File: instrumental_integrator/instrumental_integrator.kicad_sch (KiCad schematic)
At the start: 43 parts, among them CN1 282841-2, Q1 2N7002, U1 INA128, U3 LTC2358-16, U4 BAT54_C2926171, U5 BAT54_C2926171, U6 BAT54_C2926171, U7 BAT54_C2926171, U9 TLV2387DR

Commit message: added footprint links and changed instr opamp to ina828
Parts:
- removed RV1: R_Potentiometer, symbol Device:R_Potentiometer
- removed U1: INA128, symbol Amplifier_Instrumentation:INA128
- added LED1: LTST-C170GKT, easyeda2kicad:LED0805-RD_GREEN, symbol easyeda2kicad:LTST-C170GKT
- added LED5: LTST-C170TBKT, easyeda2kicad:LED0805-RD_BLUE, symbol easyeda2kicad:LTST-C170TBKT
- added LED6: LTST-C170KRKT, easyeda2kicad:LED0805-R-RD, symbol easyeda2kicad:LTST-C170KRKT
- added R27, R28: 50, symbol Device:R
- added R29: 300, symbol Device:R
- added U1: INA828IDR, easyeda2kicad:SOIC-8_L4.9-W3.9-P1.27-LS6.0-BL, symbol easyeda2kicad:INA828IDR
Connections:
- net +2V5: now also LED5.2 (A), U1.7 (+VS)
- net +5V: now also LED1.2 (+)
- net -2V5: now also LED6.2 (-), U1.4 (-VS)
- net GND: now also U3.3 (IN5-), R27.2, R28.2, R29.2, U1.5 (REF)
- net IN1: now also U1.2 (-IN)
- net IN2: now also U1.3 (+IN)
- net gain_out: now also U3.4 (IN5+)
- net at C16.1, C17.2: now also U1.6 (OUT)
- new net: LED1.1 (-), R29.1
- new net: LED5.1 (K), R27.1
- new net: LED6.1 (+), R28.1
- new net resistor chain/rg1: U1.1 (RG)
- new net resistor chain/rg2: U1.8 (RG)
- no-connect marks 51 -> 49
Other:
- added sheet resistor chain (resistorchain.kicad_sch)
- moved on the sheet: C16, C17, C2, C3, R13

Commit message: added testpoints adn +- 15V rails and resistor chain asw from previous iteration
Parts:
- added CN2: 282841-2, easyeda2kicad:CONN-TH_2P-P5.08_282841-2, symbol easyeda2kicad:282841-2
- added J1, J3, J4, J5, J6, J7, J8: Conn_01x01_Socket, TestPoint:TestPoint_THTPad_1.0x1.0mm_Drill0.5mm, symbol Connector:Conn_01x01_Socket
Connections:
- net +2V5: no longer C6.1, U3.16 (VCC)
- net +3.3V: now also H2.5
- net +5V: now also C8.2, U3.42 (VDD), U3.43 (VDD)
- net -2V5: no longer C10.1, U3.17 (VEE), U3.45 (VEE)
- net A_out: now also J7.1 (Pin_1)
- net IN1: now also CN2.1
- net IN2: now also CN2.2
- net gain_out: now also J6.1 (Pin_1)
- net intout: now reaches C1.2, Q1.3 (D), R5.2, R9.2, U9.1 (OUT1)
- net intout: now also J8.1 (Pin_1)
- net resistor chain/rg1 renamed rg1
- net rg1: now also J4.1 (Pin_1)
- net resistor chain/rg2 renamed rg2
- net rg2: now also J5.1 (Pin_1)
- new net +15V: C6.1, J1.1 (Pin_1), U3.16 (VCC)
- new net -15V: C10.1, J3.1 (Pin_1), U3.17 (VEE), U3.45 (VEE)
- no-connect marks 49 -> 48
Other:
- sheet power ports: added +15V, -15V; removed none
- note added: "Debug Test Points"
- note added: "Power LEDs"
- moved on the sheet: C8

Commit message: changed adc
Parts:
- removed C6: 0.1u, symbol Device:C
- removed C7, C8: 100n, symbol Device:C
- removed U3: LTC2358-16, Package_QFP:LQFP-48_7x7mm_P0.5mm, symbol Analog_ADC:LTC2358-16
- added C24: C_Polarized_Small_US, symbol Device:C_Polarized_Small_US
- added C25: 10uF, symbol Device:C
- added J9: Conn_Coaxial, symbol Connector:Conn_Coaxial
- added SW2: SW_DPST, symbol Switch:SW_DPST
- added SW4, SW7: SW_MEC_5G, symbol Switch:SW_MEC_5G
- added U10: ADS8681RUM, Package_DFN_QFN:QFN-16-1EP_4x4mm_P0.65mm_EP2.7x2.7mm, symbol Analog_ADC:ADS8681RUM
- C10: value 0.1u -> 10uF
- C11: value 0.1u -> 4.7uF
- C12: value 47u -> 10uF
- C9: value 2.2u -> 1uF
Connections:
- net +3.3V: now also C12.1, U10.14 (DVDD)
- net +5V: now also C25.1, U10.16 (AVDD)
- net -15V: no longer C10.1
- net A_out: now also C24.1, SW2.2, SW7.3 (B), SW7.4 (B), U10.5 (AIN_P); no longer C13.1, R9.1
- net GND: now also C10.1, C11.2, C24.2, C25.2, J9.2 (Ext), U10.1 (AGND), U10.15 (DGND), U10.17 (PAD), U10.3 (REFGND), U10.6 (AIN_GND), U10.7 (~{RST}); no longer C10.2, C11.1
- net GP16: now also J9.1 (In)
- net GP2: now also U10.10 (SCLK)
- net GP3: now also U10.8 (SDI)
- net GP4: now also U10.11 (SDO-0)
- net GP5: now also U10.12 (SDO-1)
- net GP6: now also U10.9 (CONVST/~{CS}); no longer R10.2
- net GP7: now also U10.13 (RVS)
- net GP8: now also R10.2
- net RUN: now also SW4.1 (A), SW4.2 (A); no longer H2.11
- net gain_out: now also SW2.3, SW7.1 (A), SW7.2 (A); no longer R3.1
- net at C9.2: now also C10.2, U10.4 (REFCAP)
- new net: R3.1, SW2.4
- new net: H2.11, SW4.3 (B), SW4.4 (B)
- new net: C11.1, U10.2 (REFIO)
- new net switchin: C13.1, R9.1, SW2.1
- no-connect marks 48 -> 23
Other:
- note added: "Rogowski RP2040 Connection"
- note added: "Violet Bustos Allen Chen"
- note removed: "Rogowski - Pico connection"
- note removed: "Schem by violet bustos"
- moved on the sheet: C1, C13, C14, C15, C16, C17, C2, C3, C4, C5, CN1, CN2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

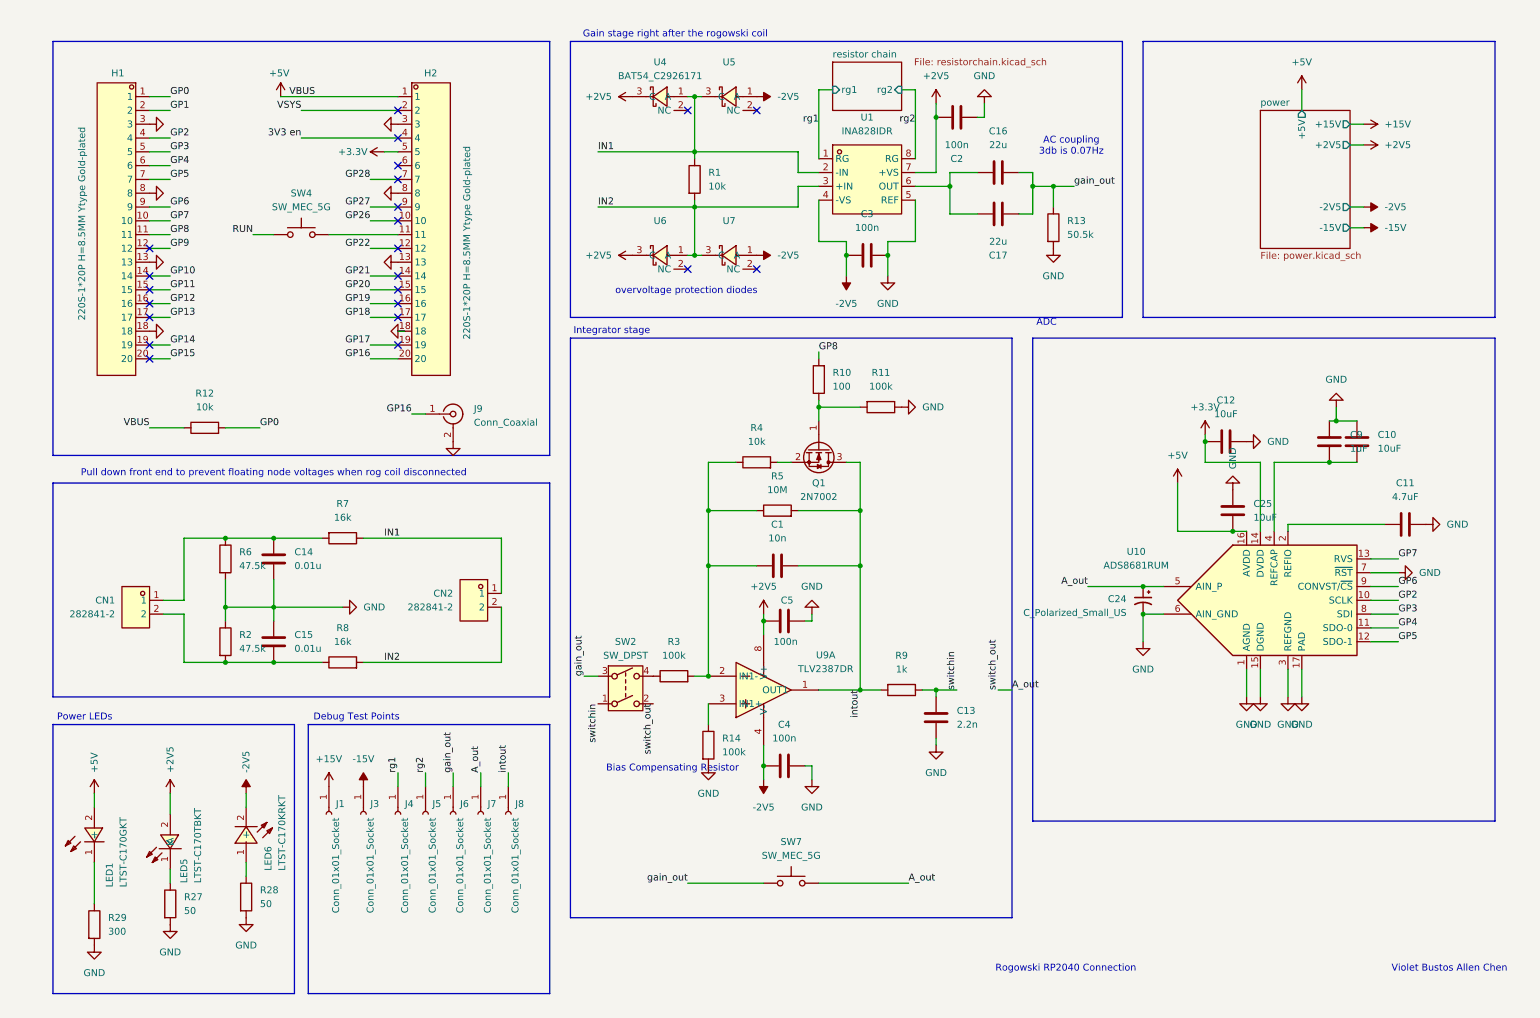
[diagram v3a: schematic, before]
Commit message: switch footprints
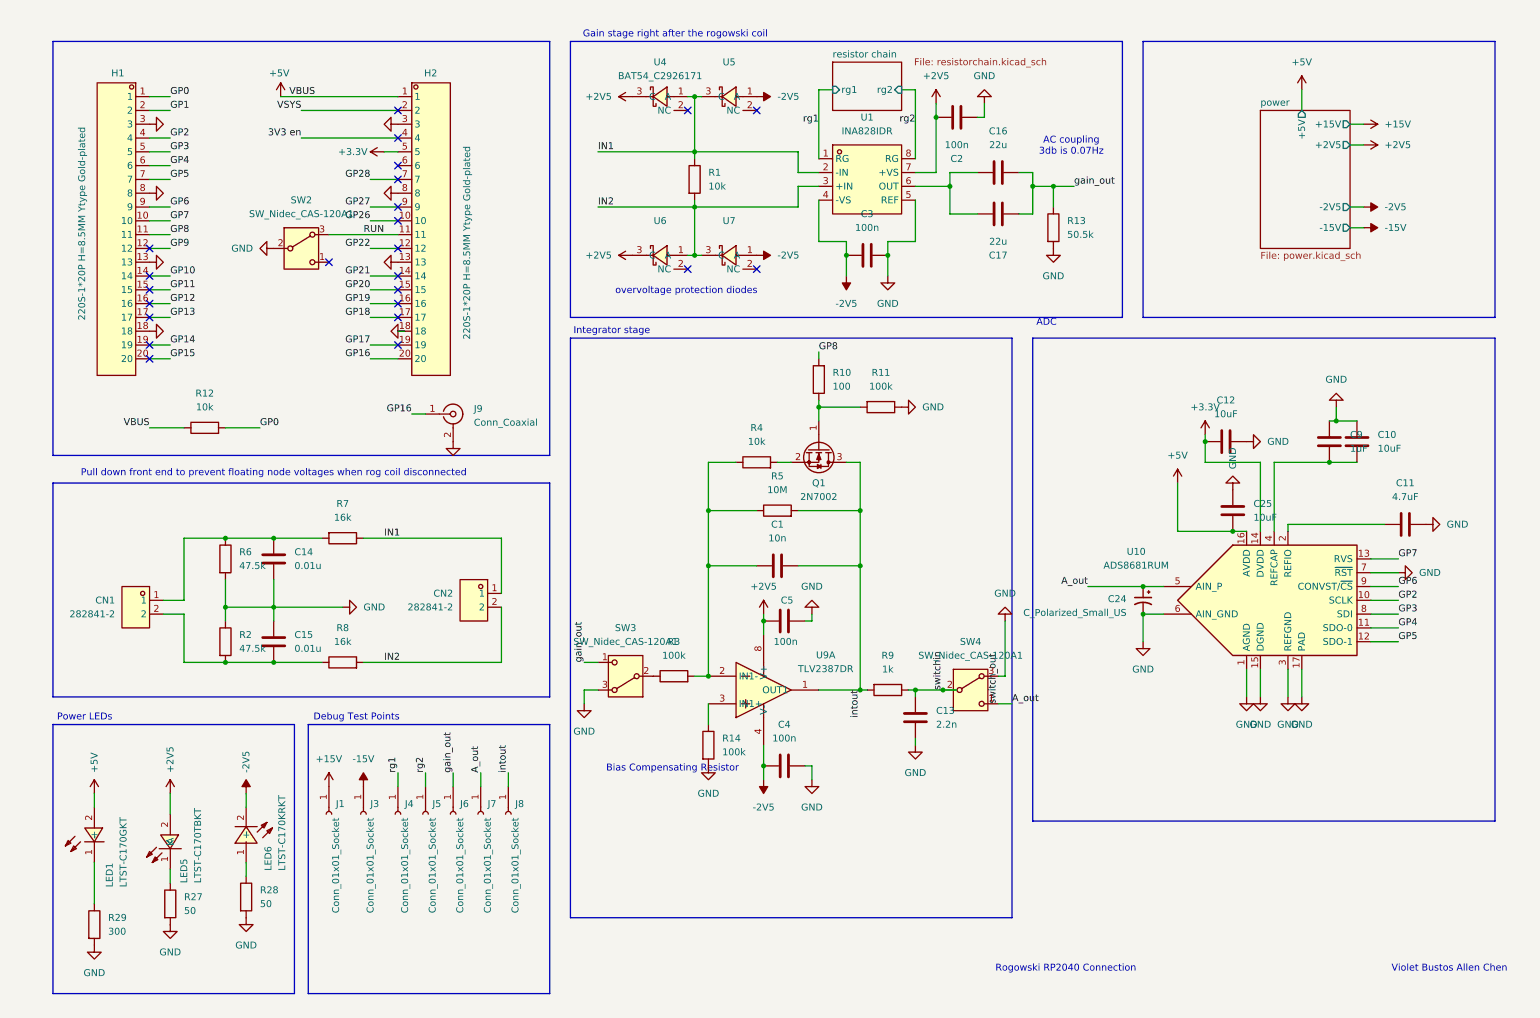
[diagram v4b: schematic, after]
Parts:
- removed SW2: SW_DPST, symbol Switch:SW_DPST
- removed SW4, SW7: SW_MEC_5G, symbol Switch:SW_MEC_5G
- added SW2, SW3, SW4: SW_Nidec_CAS-120A1, Button_Switch_SMD:Nidec_Copal_CAS-120A, symbol Switch:SW_Nidec_CAS-120A1
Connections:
- net A_out: now also SW4.1 (C)
- net GND: now also SW2.2 (B), SW3.3 (A), SW4.3 (A)
- net RUN: now also H2.11, SW2.3 (A)
- net gain_out: now also SW3.1 (C)
- net switchin: now also SW4.2 (B)
- net at R3.1: now also SW3.2 (B)
- no-connect marks 23 -> 24
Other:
- moved on the sheet: C13, R9

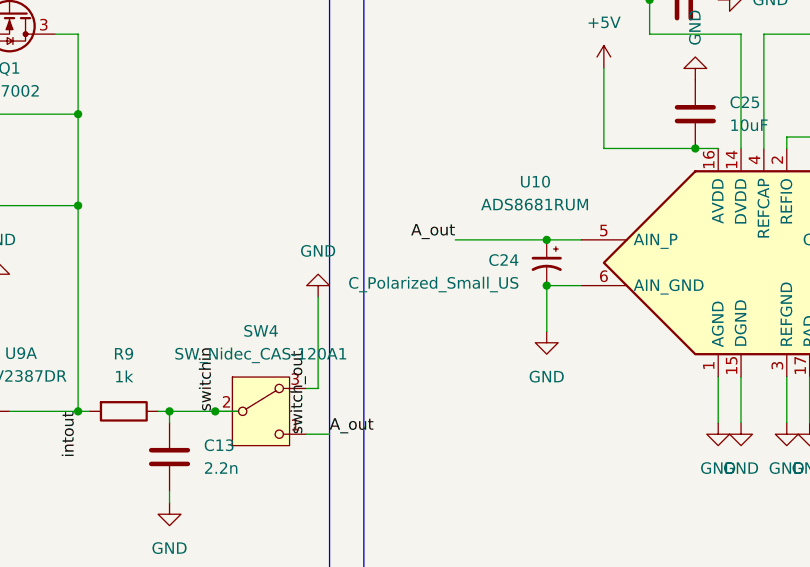
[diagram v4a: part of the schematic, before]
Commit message: switch footprints v2
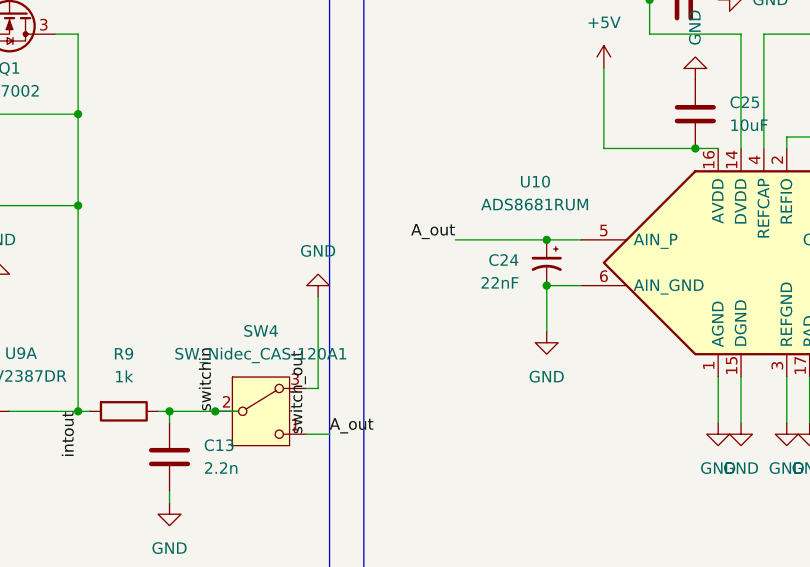
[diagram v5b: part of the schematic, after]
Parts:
- C24: value C_Polarized_Small_US -> 22nF
- CN1, CN2: Manufacturer TE Connectivity(泰科电子) -> (none)
- H1, H2: Manufacturer Ckmtw(灿科盟) -> (none)
- LED1, LED5, LED6: Manufacturer LITEON(光宝) -> (none)
- U1, U9: Manufacturer TI(德州仪器) -> (none)
- U4, U5, U6, U7: Manufacturer FOSAN(富捷/富信) -> (none)

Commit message: added stuff, removedf some stuff
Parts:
- removed C14, C15: 0.01u, symbol Device:C
- removed CN1: 282841-2, easyeda2kicad:CONN-TH_2P-P5.08_282841-2, symbol easyeda2kicad:282841-2
- removed J1, J3: Conn_01x01_Socket, TestPoint:TestPoint_THTPad_1.0x1.0mm_Drill0.5mm, symbol Connector:Conn_01x01_Socket
- removed R2, R6: 47.5k, symbol Device:R
- removed R7, R8: 16k, symbol Device:R
- removed SW2: SW_Nidec_CAS-120A1, Button_Switch_SMD:Nidec_Copal_CAS-120A, symbol Switch:SW_Nidec_CAS-120A1
- added SW2: TS1603-TZ38HBM, easyeda2kicad:SW-SMD_4P-L4.5-W4.5-P3.00-LS6.8, symbol easyeda2kicad:TS1603-TZ38HBM
- R3: value 100k -> 15k
- R5: value 10M -> 1M
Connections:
- net A_out: now also SW4.2 (B); no longer SW4.1 (C)
- net GND: now also SW2.1 (A); no longer SW4.3 (A)
- net RUN: now also SW2.4 (D)
- net gain_out: now also SW4.3 (A)
- net switchin: now also SW4.1 (C); no longer SW4.2 (B)
- no-connect marks 24 -> 25
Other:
- sheet power ports: added none; removed +15V, -15V
- note added: "Connector"
- note removed: "Pull down front end to prevent floating node voltages when rog coil disconnected"
- moved on the sheet: CN2, J4, J5, J6, J7, J8, SW4

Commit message: yurrp
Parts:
- R14: value 100k -> 14.8k
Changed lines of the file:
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@@
 	(rectangle
 		(start 110.49 73.66)
-		(end 198.12 180.34)
+		(end 198.12 165.1)
 		(stroke
 			(width 0)
@@
 			)
 		)
-		(property "Value" "100k"
+		(property "Value" "14.8k"
 			(at 138.43 149.8599 0)
 			(show_name no)

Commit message: started pcb
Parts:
- removed C16, C17: 22u, symbol Device:C
- removed J9: Conn_Coaxial, symbol Connector:Conn_Coaxial
- removed SW3, SW4: SW_Nidec_CAS-120A1, Button_Switch_SMD:Nidec_Copal_CAS-120A, symbol Switch:SW_Nidec_CAS-120A1
- added CN3: 282841-2, easyeda2kicad:CONN-TH_2P-P5.08_282841-2, symbol easyeda2kicad:282841-2
- added J10, J12, J13, J14, J15, J16, J9: Conn_01x01_Socket, TestPoint:TestPoint_THTPad_1.0x1.0mm_Drill0.5mm, symbol Connector:Conn_01x01_Socket
- added LED7: LTST-C170TBKT, easyeda2kicad:LED0805-RD_BLUE, symbol easyeda2kicad:LTST-C170TBKT
- added R30: 50, Resistor_SMD:R_0805_2012Metric, symbol Device:R
- added R6: 5k, Resistor_SMD:R_0805_2012Metric, symbol Device:R
- added RF1: KH-BNC50-3511, easyeda2kicad:ANT-TH_KH-BNC50-3511, symbol easyeda2kicad:KH-BNC50-3511
- added U11, U12: SS12D10G5, easyeda2kicad:SW-TH_SHOU-HAN_SS12D10G4, symbol easyeda2kicad:SS12D10G5
- added U2, U3: C3D22UF500V82CB0300, easyeda2kicad:CAP-TH_L32.0-W22.0-P27.50-D1.3, symbol easyeda2kicad:C3D22UF500V82CB0300
- C1: footprint (none) -> Capacitor_SMD:C_0603_1608Metric
- C10, C11, C13, C2, C3, C4, C5, C9: footprint (none) -> Capacitor_SMD:C_0805_2012Metric
- C12, C25: value 10uF -> 1uF; footprint (none) -> Capacitor_SMD:C_0603_1608Metric
- C24: footprint (none) -> Capacitor_SMD:C_1206_3216Metric
- R1: value 10k -> 5k; footprint (none) -> Resistor_SMD:R_0805_2012Metric
- R10, R11, R12, R13, R14, R27, R28, R29, R3, R4, R5, R9: footprint (none) -> Resistor_SMD:R_0805_2012Metric
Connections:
- net +3.3V: now also LED7.2 (A)
- net A_out: now also U12.2
- net GND: now also R1.2, CN3.2, J10.1 (Pin_1), R30.2, R6.2, RF1.1 (OUT), U11.1
- net GP16: now also RF1.2
- net GP2: now also J14.1 (Pin_1)
- net GP3: now also J13.1 (Pin_1)
- net GP4: now also J12.1 (Pin_1)
- net GP5: now also J9.1 (Pin_1)
- net GP6: now also J15.1 (Pin_1)
- net GP7: now also J16.1 (Pin_1)
- net IN2: now also R6.1; no longer R1.2
- net gain_out: now also CN3.1, U11.3, U12.3, U2.2, U3.2
- net switchin: now also U12.1
- net opin-: now reaches C1.1, R3.2, R4.1, R5.1, U9.2 (IN1-)
- net at R3.1: now also U11.2
- net at U1.6 (OUT): now also U2.1, U3.1
- net opin+: now reaches R14.1, U9.3 (IN1+)
- new net: LED7.1 (K), R30.1
- no-connect marks 25 -> 27
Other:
- note added: "22u"
- moved on the sheet: J4, J5, J6, J7, J8, LED6, R28
